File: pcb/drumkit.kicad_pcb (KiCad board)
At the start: 2 copper layers, 118.7 x 90.8 mm, 26 parts, among them J1 BATTERY, J2 Conn_01x04_Female, SW1 BUTTON1, SW2 BUTTON2, SW3 BUTTON3, SW4 BUTTON4, SW5 POWER_SW, U1 Pico

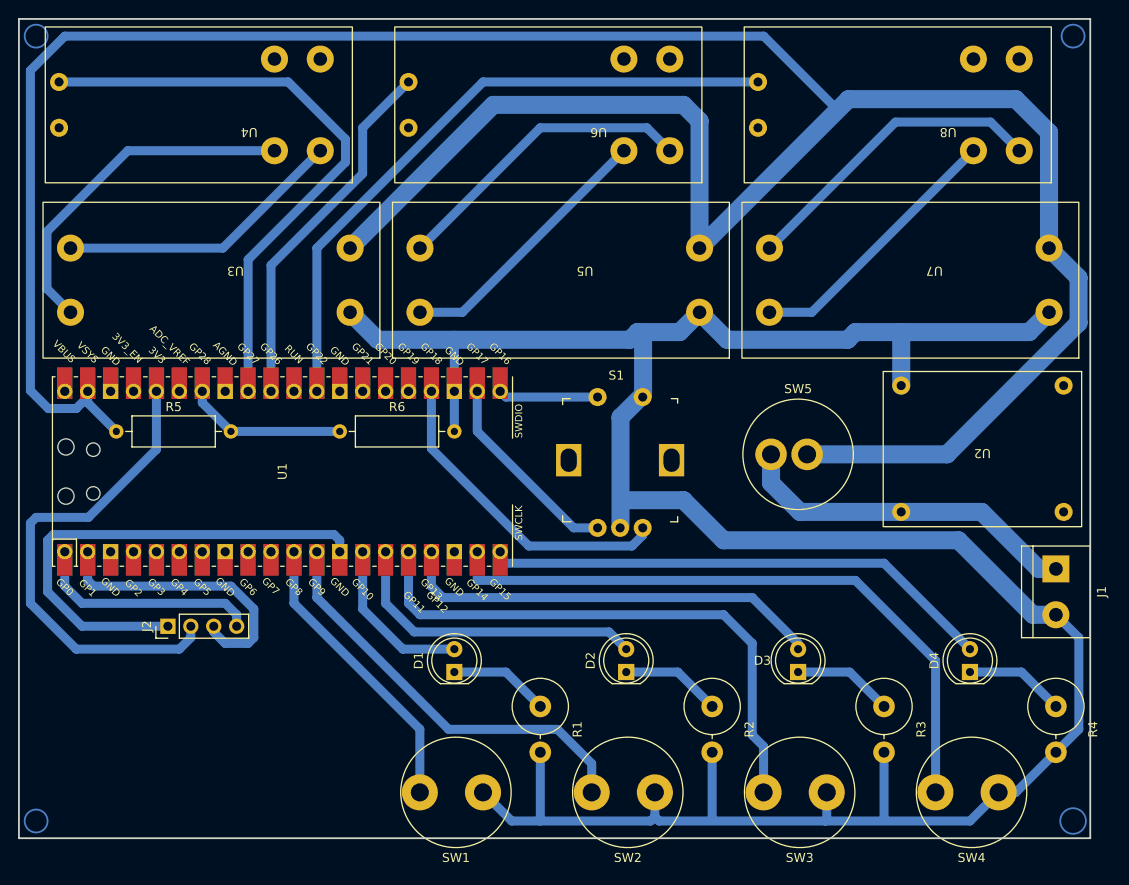
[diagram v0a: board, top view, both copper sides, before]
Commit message: squeeze in safety diodes
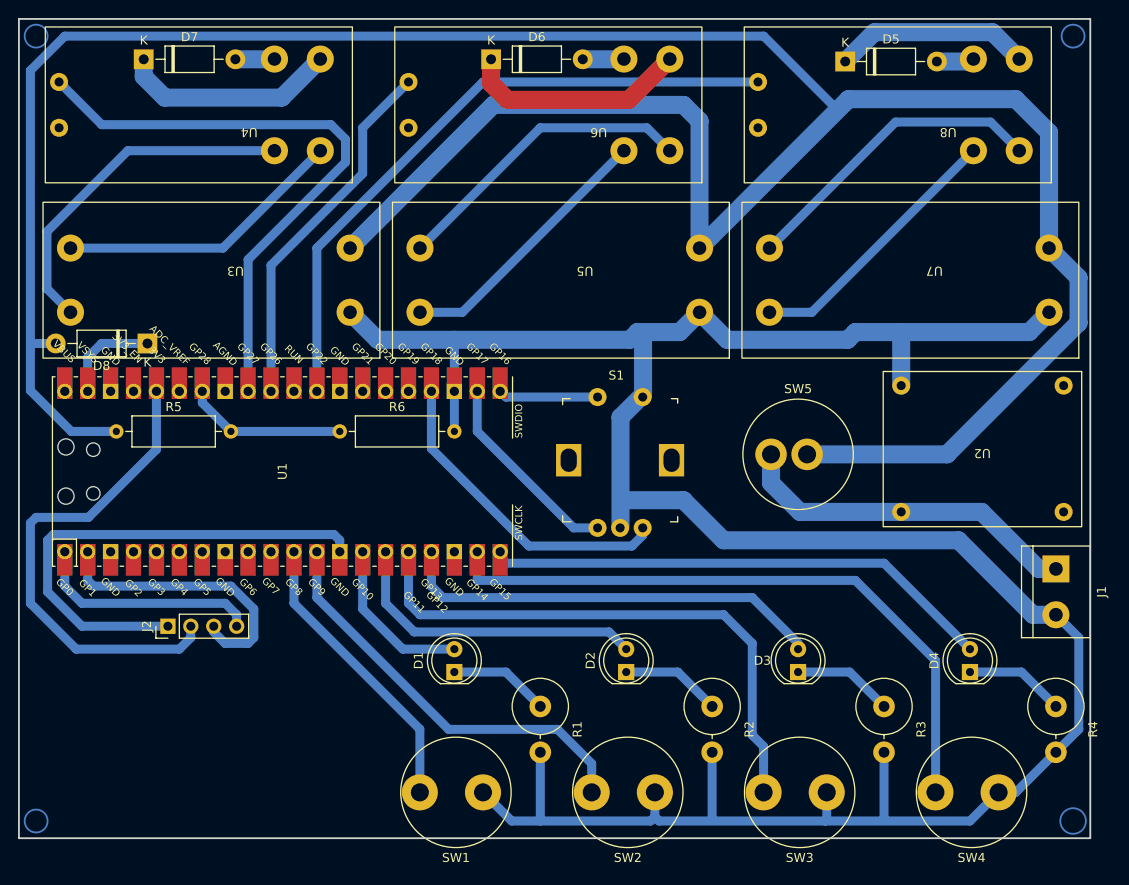
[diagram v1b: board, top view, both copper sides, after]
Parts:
- added D5: 1N5819, Diode_THT:D_DO-41_SOD81_P10.16mm_Horizontal, F.Cu at (181.7, 55.2)
- added D6: 1N5819, Diode_THT:D_DO-41_SOD81_P10.16mm_Horizontal, F.Cu at (142.4, 55.0)
- added D7: 1N5819, Diode_THT:D_DO-41_SOD81_P10.16mm_Horizontal, F.Cu at (103.9, 55.0)
- added D8: 1N5819, Diode_THT:D_DO-41_SOD81_P10.16mm_Horizontal, F.Cu at (104.3, 86.5)
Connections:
- U1 pad 39: +BATT -> Net-(D8-K)
- U4 pad 3: unconnected-(U4-Out+-Pad3) -> Net-(D7-K)
- U4 pad 4: unconnected-(U4-Out--Pad4) -> Net-(D7-A)
- U6 pad 3: unconnected-(U6-Out+-Pad3) -> Net-(D6-K)
- U6 pad 4: unconnected-(U6-Out--Pad4) -> Net-(D6-A)
- U8 pad 3: unconnected-(U8-Out+-Pad3) -> Net-(D5-K)
- U8 pad 4: unconnected-(U8-Out--Pad4) -> Net-(D5-A)
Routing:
- net Net-(D6-K): track 0.00 -> 25.1 mm
- net Net-(D7-K): track 0.00 -> 24.2 mm
- net Net-(D5-K): track 0.00 -> 21.9 mm
- net Net-(D8-K): track 0.00 -> 11.0 mm
- net Net-(D6-A): track 0.00 -> 4.58 mm
- net Net-(D7-A): track 0.00 -> 4.34 mm
- net Net-(D5-A): track 0.00 -> 4.16 mm

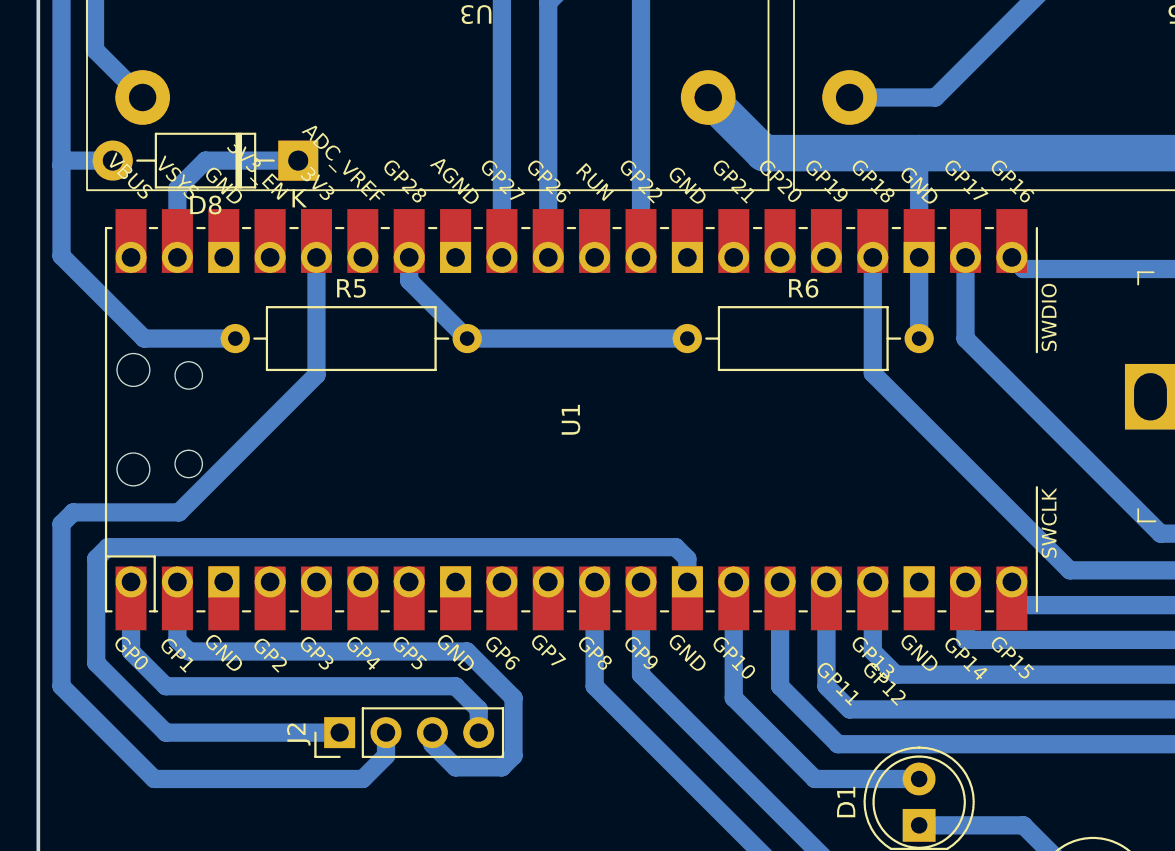
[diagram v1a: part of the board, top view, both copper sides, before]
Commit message: add 3d model to prototype pcb
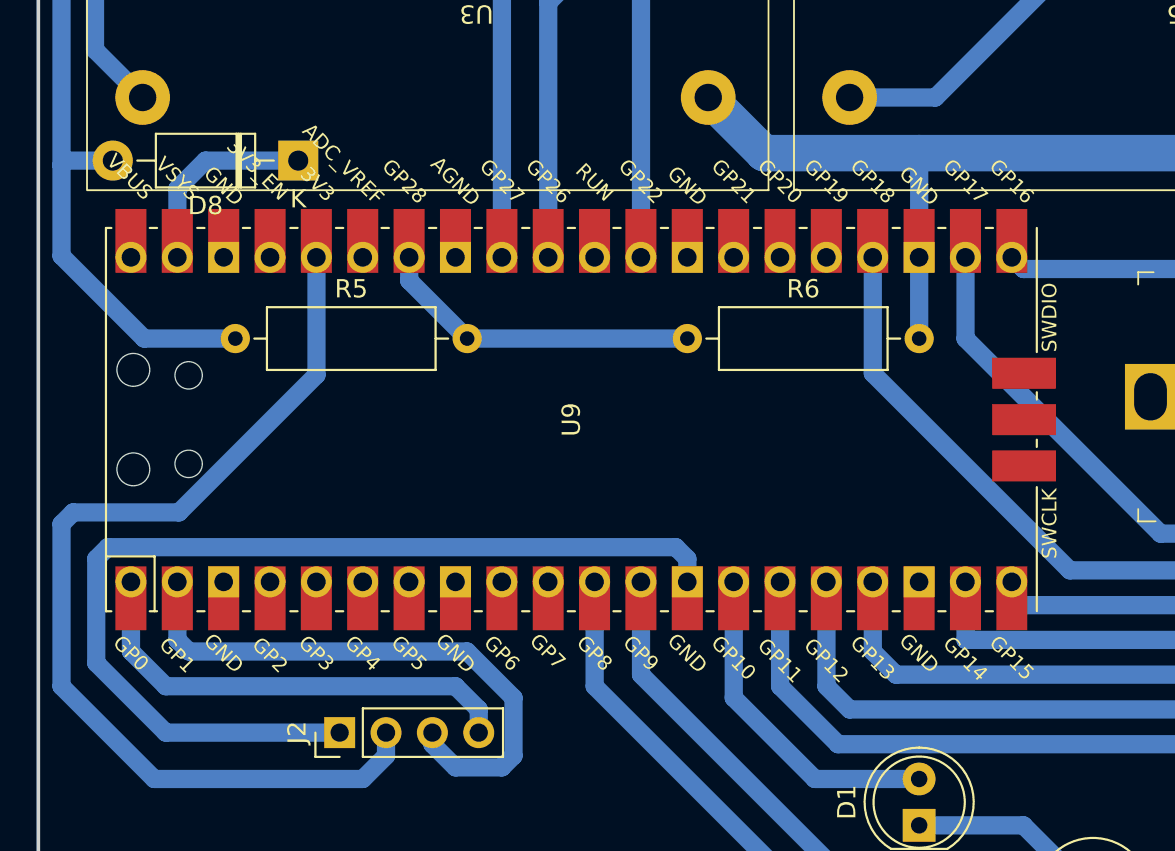
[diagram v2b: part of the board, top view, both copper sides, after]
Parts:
- removed U1: Pico, MCU_RaspberryPi_and_Boards:RPi_Pico_SMD_TH
- added U9: Pico, KiCad-RP-Pico:RPi_Pico_SMD_TH_noSWD, F.Cu at (119.3, 100.7)
